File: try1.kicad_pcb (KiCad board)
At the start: 2 copper layers, 175.3 x 119.4 mm, 33 parts, among them J10 Archon-connector-modules-Driv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, J11 Archon-connector-modules-Driv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, J2 Archon-connector-modules-Heat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, J21 DB37, J22 DB37, J3 Archon-connector-modules-Driv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, J31 DB9, J4 Archon-connector-modules-LVBi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, J41 CONN_DVI, J5 Archon-connector-modules-ADC, J6 Archon-connector-modules-ADC, J7 Archon-connector-modules-ADC, J8 Archon-connector-modules-ADC, J9 Archon-connector-modules-HVBi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, P1 CONN_02X02

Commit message: PCB Layout Fix-Ups
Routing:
- net /~ResetLog_R: track 97.7 -> 94.7 mm
- net /P3X: track 83.1 -> 85.8 mm
- net /TGX: track 88.7 -> 91.1 mm
- net /P2X: track 78.2 -> 80.3 mm
- net /VLg_L: track 88.9 -> 86.9 mm
- net /P1X: track 74.6 -> 76.0 mm
- net /ResetLO_L: track 94.7 -> 95.6 mm
- net /-15V_L: track 100.3 -> 101.1 mm
- net FLASH_V: track 58.8 -> 59.3 mm

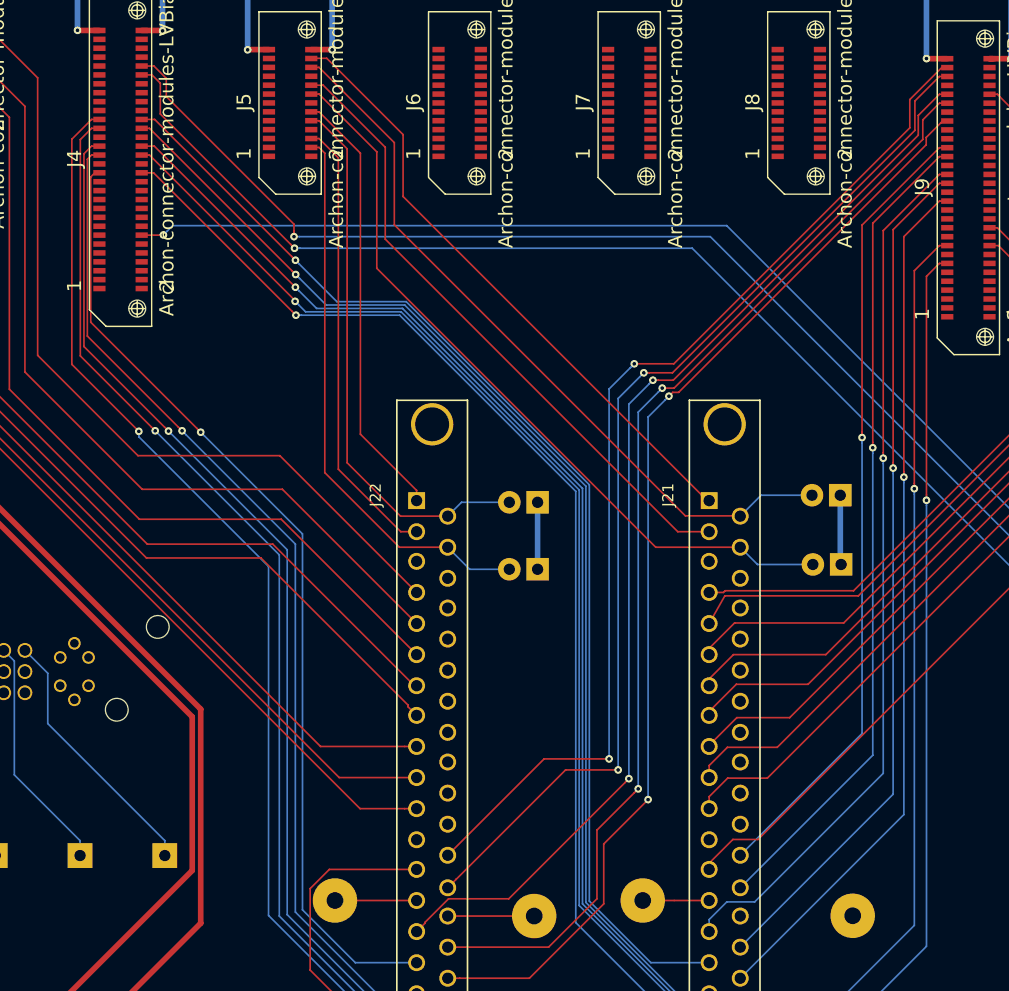
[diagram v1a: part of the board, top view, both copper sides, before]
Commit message: Fine Tuning Traces
This may not be final, but as I fix up the traces, the other traces
look bad by comparison so I keep tweaking things.  I can't help
myself.
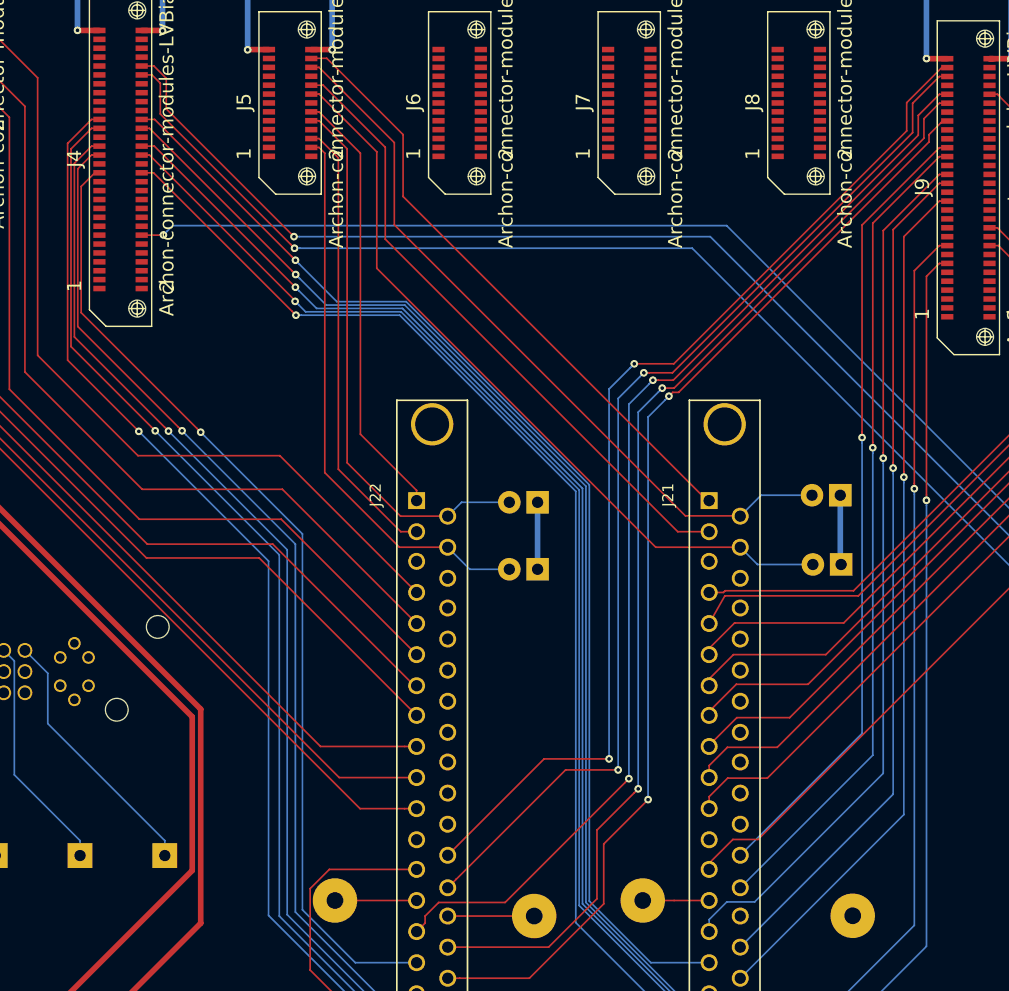
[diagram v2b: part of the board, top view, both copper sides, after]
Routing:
- net /GainSW2_L: track 90.6 -> 91.3 mm
- net /VLg_L: track 86.9 -> 87.6 mm
- net /ResetLO_L: track 95.6 -> 96.3 mm
- net /+15V_L: track 95.7 -> 96.4 mm

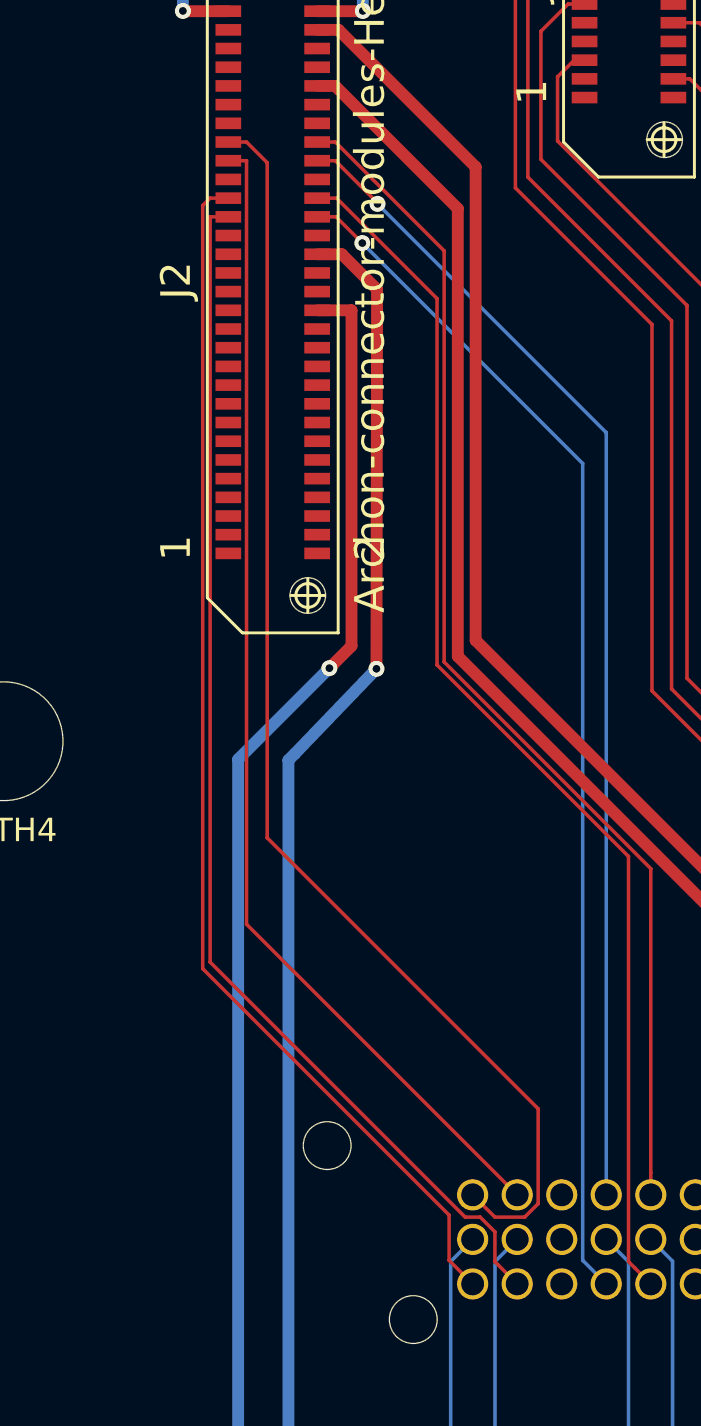
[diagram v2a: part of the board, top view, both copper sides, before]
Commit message: Tweak Heater Traces
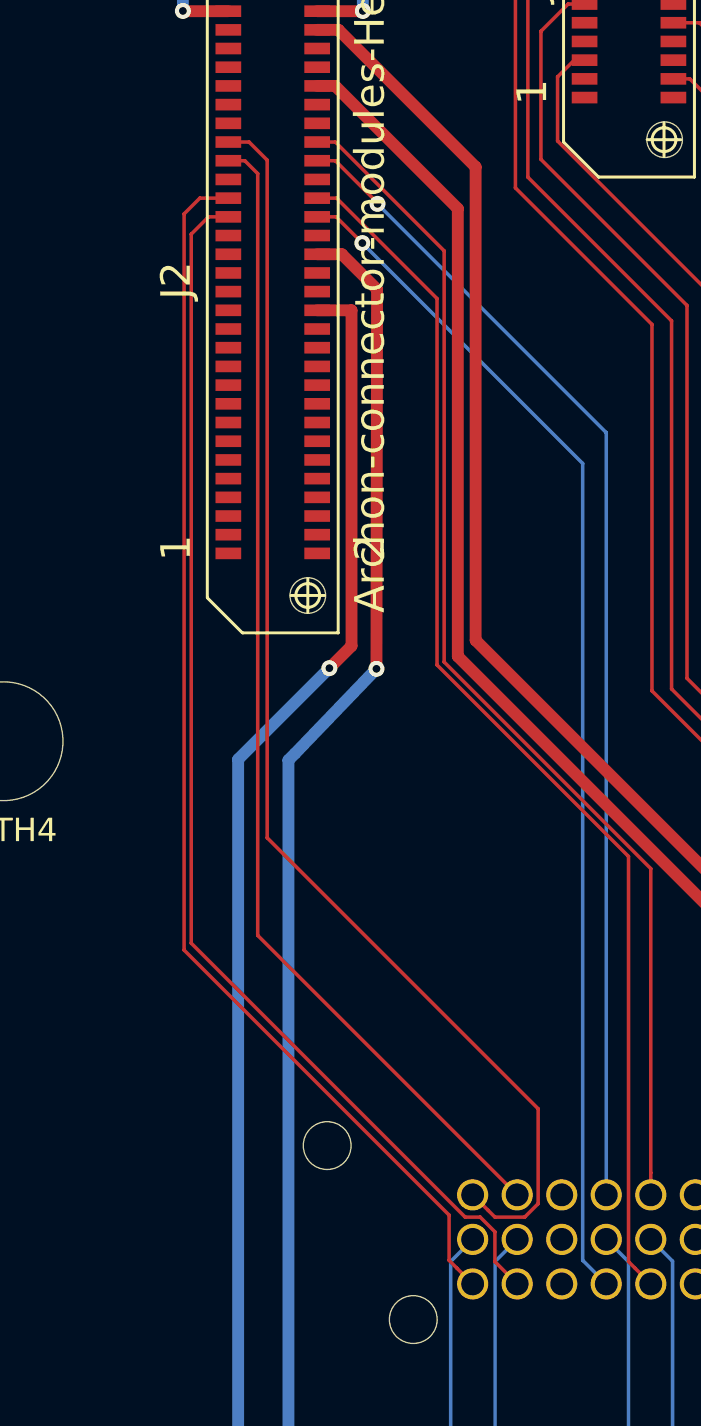
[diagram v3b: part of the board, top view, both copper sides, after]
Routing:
- net HEATER1_TEMPA_FN: track 52.1 -> 53.1 mm
- net HEATER1_TEMPA_FP: track 52.2 -> 53.0 mm
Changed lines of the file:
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@@
     (thickness 1.6)
     (drawings 9)
-    (tracks 681)
+    (tracks 685)
     (zones 0)
     (modules 33)
@@
   (segment (start 65.5541 69.3595) (end 65.2716 69.642) (width 0.508) (layer B.Cu) (net 33))
   (segment (start 65.5541 69.3595) (end 69.0372 65.7352) (width 0.508) (layer B.Cu) (net 33))
-  (segment (start 74.1045 91.0971) (end 75.057 92.0496) (width 0.1524) (layer F.Cu) (net 36) (status 20))
+  (segment (start 62.7001 46.4009) (end 61.8539 46.4009) (width 0.1524) (layer F.Cu) (net 36))
+  (segment (start 61.8539 46.4009) (end 61.1124 47.1424) (width 0.1524) (layer F.Cu) (net 36))
+  (segment (start 61.1124 47.1424) (end 61.1124 77.4721) (width 0.1524) (layer F.Cu) (net 36))
+  (segment (start 61.1124 77.4721) (end 72.8324 89.1921) (width 0.1524) (layer F.Cu) (net 36))
+  (segment (start 72.8324 89.1921) (end 73.4755 89.1921) (width 0.1524) (layer F.Cu) (net 36))
   (segment (start 74.1045 89.8211) (end 74.1045 91.0971) (width 0.1524) (layer F.Cu) (net 36))
+  (segment (start 74.1045 91.0971) (end 75.057 92.0496) (width 0.1524) (layer F.Cu) (net 36))
   (segment (start 73.4755 89.1921) (end 74.1045 89.8211) (width 0.1524) (layer F.Cu) (net 36))
-  (segment (start 72.8324 89.1921) (end 73.4755 89.1921) (width 0.1524) (layer F.Cu) (net 36))
-  (segment (start 61.9213 78.281) (end 72.8324 89.1921) (width 0.1524) (layer F.Cu) (net 36))
-  (segment (start 61.9213 46.4009) (end 61.9213 78.281) (width 0.1524) (layer F.Cu) (net 36))
-  (segment (start 62.7001 46.4009) (end 61.9213 46.4009) (width 0.1524) (layer F.Cu) (net 36) (status 10))
   (segment (start 77.859 56.94972) (end 68.43268 47.5234) (width 0.1524) (layer B.Cu) (net 37))
   (segment (start 77.859 91.0416) (end 77.859 56.94972) (width 0.1524) (layer B.Cu) (net 37))
@@
   (segment (start 66.4999 46.4009) (end 67.31018 46.4009) (width 0.1524) (layer F.Cu) (net 37) (status 10))
   (via (at 68.43268 47.5234) (size 0.6858) (drill 0.3302) (layers F.Cu B.Cu) (net 37))
-  (segment (start 72.144 91.0416) (end 73.152 92.0496) (width 0.1524) (layer F.Cu) (net 38) (status 20))
+  (segment (start 72.485251 91.382851) (end 73.152 92.0496) (width 0.1524) (layer F.Cu) (net 38))
+  (segment (start 72.144 91.0416) (end 72.485251 91.382851) (width 0.1524) (layer F.Cu) (net 38))
+  (segment (start 62.7001 45.6008) (end 61.481433 45.6008) (width 0.1524) (layer F.Cu) (net 38))
   (segment (start 72.144 89.1036) (end 72.144 91.0416) (width 0.1524) (layer F.Cu) (net 38))
-  (segment (start 61.6048 78.5644) (end 72.144 89.1036) (width 0.1524) (layer F.Cu) (net 38))
-  (segment (start 61.6048 45.9173) (end 61.6048 78.5644) (width 0.1524) (layer F.Cu) (net 38))
-  (segment (start 61.9213 45.6008) (end 61.6048 45.9173) (width 0.1524) (layer F.Cu) (net 38))
-  (segment (start 62.7001 45.6008) (end 61.9213 45.6008) (width 0.1524) (layer F.Cu) (net 38) (status 10))
+  (segment (start 60.807589 77.767189) (end 72.144 89.1036) (width 0.1524) (layer F.Cu) (net 38))
+  (segment (start 60.807589 46.274644) (end 60.807589 77.767189) (width 0.1524) (layer F.Cu) (net 38))
+  (segment (start 61.481433 45.6008) (end 60.807589 46.274644) (width 0.1524) (layer F.Cu) (net 38))
   (segment (start 67.331691 45.6008) (end 71.627956 49.897065) (width 0.1524) (layer F.Cu) (net 39))
   (segment (start 71.627956 49.897065) (end 71.627956 65.570022) (width 0.1524) (layer F.Cu) (net 39))
@@
   (segment (start 80.103981 91.381581) (end 80.772 92.0496) (width 0.1524) (layer F.Cu) (net 39))
   (segment (start 66.4999 45.6008) (end 67.331691 45.6008) (width 0.1524) (layer F.Cu) (net 39))
-  (segment (start 63.4789 76.6615) (end 75.057 88.2396) (width 0.1524) (layer F.Cu) (net 42) (status 20))
-  (segment (start 63.4789 44.0006) (end 63.4789 76.6615) (width 0.1524) (layer F.Cu) (net 42))
-  (segment (start 62.7001 44.0006) (end 63.4789 44.0006) (width 0.1524) (layer F.Cu) (net 42) (status 10))
+  (segment (start 62.7001 44.0006) (end 63.4062 44.0006) (width 0.1524) (layer F.Cu) (net 42))
+  (segment (start 63.4062 44.0006) (end 63.9572 44.5516) (width 0.1524) (layer F.Cu) (net 42))
+  (segment (start 63.9572 44.5516) (end 63.9572 77.1398) (width 0.1524) (layer F.Cu) (net 42))
+  (segment (start 63.9572 77.1398) (end 75.057 88.2396) (width 0.1524) (layer F.Cu) (net 42))
   (via (at 69.082 45.8458) (size 0.6858) (layers F.Cu B.Cu) (net 43))
   (segment (start 78.867 55.6308) (end 69.082 45.8458) (width 0.1524) (layer B.Cu) (net 43))
@@
   (segment (start 67.2787 44.0006) (end 69.082 45.8039) (width 0.1524) (layer F.Cu) (net 43))
   (segment (start 66.4999 44.0006) (end 67.2787 44.0006) (width 0.1524) (layer F.Cu) (net 43) (status 10))
-  (segment (start 74.1045 89.1921) (end 73.152 88.2396) (width 0.1524) (layer F.Cu) (net 44) (status 20))
-  (segment (start 75.3775 89.1921) (end 74.1045 89.1921) (width 0.1524) (layer F.Cu) (net 44))
+  (segment (start 73.820019 88.907619) (end 73.152 88.2396) (width 0.1524) (layer F.Cu) (net 44))
+  (segment (start 74.1045 89.1921) (end 73.820019 88.907619) (width 0.1524) (layer F.Cu) (net 44))
   (segment (start 75.954 88.6156) (end 75.3775 89.1921) (width 0.1524) (layer F.Cu) (net 44))
   (segment (start 75.954 84.5561) (end 75.954 88.6156) (width 0.1524) (layer F.Cu) (net 44))
   (segment (start 64.3619 72.964) (end 75.954 84.5561) (width 0.1524) (layer F.Cu) (net 44))
-  (segment (start 64.3619 44.0835) (end 64.3619 72.964) (width 0.1524) (layer F.Cu) (net 44))
-  (segment (start 63.4789 43.2005) (end 64.3619 44.0835) (width 0.1524) (layer F.Cu) (net 44))
-  (segment (start 62.7001 43.2005) (end 63.4789 43.2005) (width 0.1524) (layer F.Cu) (net 44) (status 10))
+  (segment (start 64.3619 43.974233) (end 64.3619 72.964) (width 0.1524) (layer F.Cu) (net 44))
+  (segment (start 63.588167 43.2005) (end 64.3619 43.974233) (width 0.1524) (layer F.Cu) (net 44))
+  (segment (start 75.3775 89.1921) (end 74.1045 89.1921) (width 0.1524) (layer F.Cu) (net 44))
+  (segment (start 62.7001 43.2005) (end 63.588167 43.2005) (width 0.1524) (layer F.Cu) (net 44))
   (segment (start 71.932767 65.443766) (end 80.772 74.282998) (width 0.1524) (layer F.Cu) (net 45))
   (segment (start 80.772 74.282998) (end 80.772 87.294878) (width 0.1524) (layer F.Cu) (net 45))

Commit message: Adjust Silks, Names
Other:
- board text added: "Morley Blouke Denis Heidtmann Paul DeStefano"
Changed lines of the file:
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@@
     (area 41.951046 18.373109 222.731954 142.492701)
     (thickness 1.6)
-    (drawings 9)
+    (drawings 10)
     (tracks 685)
     (zones 0)
@@
       (effects (font (size 1.27 1.27) (thickness 0.1016)))
     )
-    (fp_text value Archon-connector-modules-LVBias (at 0.90932 4.16306 90) (layer F.SilkS)
+    (fp_text value Archon-connector-modules-LVBias (at 0.7622 5.504 90) (layer F.SilkS)
       (effects (font (size 1.27 1.27) (thickness 0.1016)))
     )
@@
       (effects (font (size 1.27 1.27) (thickness 0.1016)))
     )
-    (fp_text value Archon-connector-modules-Heater (at 0.90932 4.16306 90) (layer F.SilkS)
+    (fp_text value Archon-connector-modules-Heater (at 1.1432 5.3008 90) (layer F.SilkS)
       (effects (font (size 1.27 1.27) (thickness 0.1016)))
     )
@@
       (effects (font (size 1.27 1.27) (thickness 0.1016)))
     )
-    (fp_text value Archon-connector-modules-ADC (at 0.90932 4.16306 90) (layer F.SilkS)
+    (fp_text value Archon-connector-modules-ADC (at -0.584 5.4024 90) (layer F.SilkS)
       (effects (font (size 1.27 1.27) (thickness 0.1016)))
     )
@@
       (effects (font (size 1.27 1.27) (thickness 0.1016)))
     )
-    (fp_text value Archon-connector-modules-ADC (at 0.90932 4.16306 90) (layer F.SilkS)
+    (fp_text value Archon-connector-modules-ADC (at -0.3554 5.8342 90) (layer F.SilkS)
       (effects (font (size 1.27 1.27) (thickness 0.1016)))
     )
@@
       (effects (font (size 1.27 1.27) (thickness 0.1016)))
     )
-    (fp_text value Archon-connector-modules-ADC (at 0.90932 4.16306 90) (layer F.SilkS)
+    (fp_text value Archon-connector-modules-ADC (at -0.2538 5.7072 90) (layer F.SilkS)
       (effects (font (size 1.27 1.27) (thickness 0.1016)))
     )
@@
       (effects (font (size 1.27 1.27) (thickness 0.1016)))
     )
-    (fp_text value Archon-connector-modules-ADC (at 0.90932 4.16306 90) (layer F.SilkS)
+    (fp_text value Archon-connector-modules-ADC (at -1.0158 5.3008 90) (layer F.SilkS)
       (effects (font (size 1.27 1.27) (thickness 0.1016)))
     )
@@
       (effects (font (size 1.27 1.27) (thickness 0.1016)))
     )
-    (fp_text value Archon-connector-modules-Driver (at 0.90932 4.16306 90) (layer F.SilkS)
+    (fp_text value Archon-connector-modules-Driver (at -4.1654 6.3168 90) (layer F.SilkS)
       (effects (font (size 1.27 1.27) (thickness 0.1016)))
     )
@@
       (effects (font (size 1.27 1.27) (thickness 0.1016)))
     )
-    (fp_text value Archon-connector-modules-Driver (at 0.90932 4.16306 90) (layer F.SilkS)
+    (fp_text value Archon-connector-modules-Driver (at -3.9622 5.9304 90) (layer F.SilkS)
       (effects (font (size 1.27 1.27) (thickness 0.1016)))
     )
@@
       (effects (font (size 1.27 1.27) (thickness 0.1016)))
     )
-    (fp_text value Archon-connector-modules-Driver (at 0.90932 4.16306 90) (layer F.SilkS)
+    (fp_text value Archon-connector-modules-Driver (at -4.14 5.5548 90) (layer F.SilkS)
       (effects (font (size 1.27 1.27) (thickness 0.1016)))
     )
@@
     (pad "" np_thru_hole circle (at -6.6 1.524 90) (size 1.524 1.524) (drill 1.524) (layers *.Cu *.Mask F.SilkS))
   )
+  (gr_text "Morley Blouke\nDenis Heidtmann\nPaul DeStefano" (at 197.6374 122.1486) (layer F.SilkS)
+    (effects (font (size 1.5 1.5) (thickness 0.3)))
+  )
   (gr_text Y (at 123.2916 136.779) (layer B.SilkS)
